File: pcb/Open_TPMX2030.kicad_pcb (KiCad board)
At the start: 0 parts

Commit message: feat: Adjusting the project for a successful start
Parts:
- added D1: 1N4148W, Diode_SMD:D_SOD-123, F.Cu at (146.2, 81.0)
- added G***: LOGO, Open_TPMX2030:Artilect-Logo_12x19mm, F.Cu at (160.0, 82.5)
- added SW1: SW_Push, PCM_Switch_Keyboard_Hotswap_Kailh:SW_Hotswap_Kailh_Choc_V1V2_1.00u, F.Cu at (146.0, 65.0)
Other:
- board outline added: 250 x 102 mm
- copper layers 0 -> 2

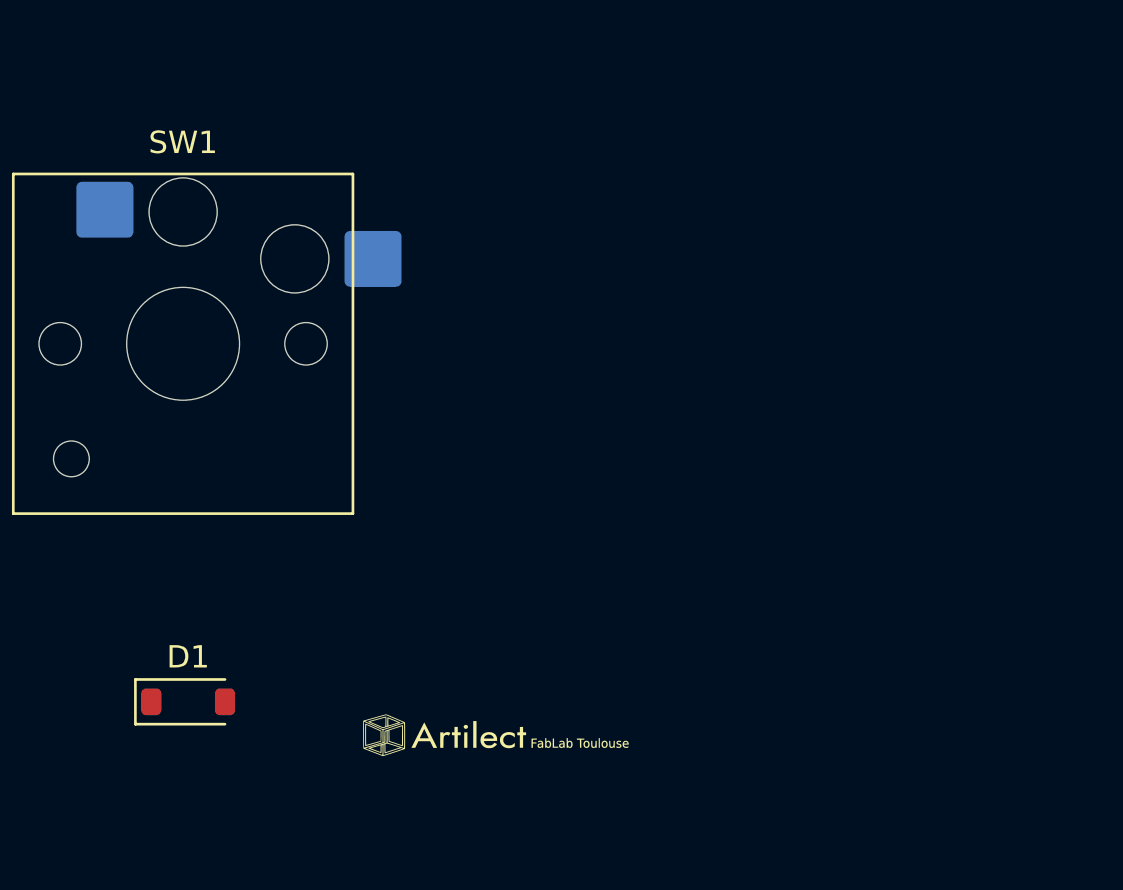
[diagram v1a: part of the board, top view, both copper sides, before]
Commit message: feat: place two switch version for testing
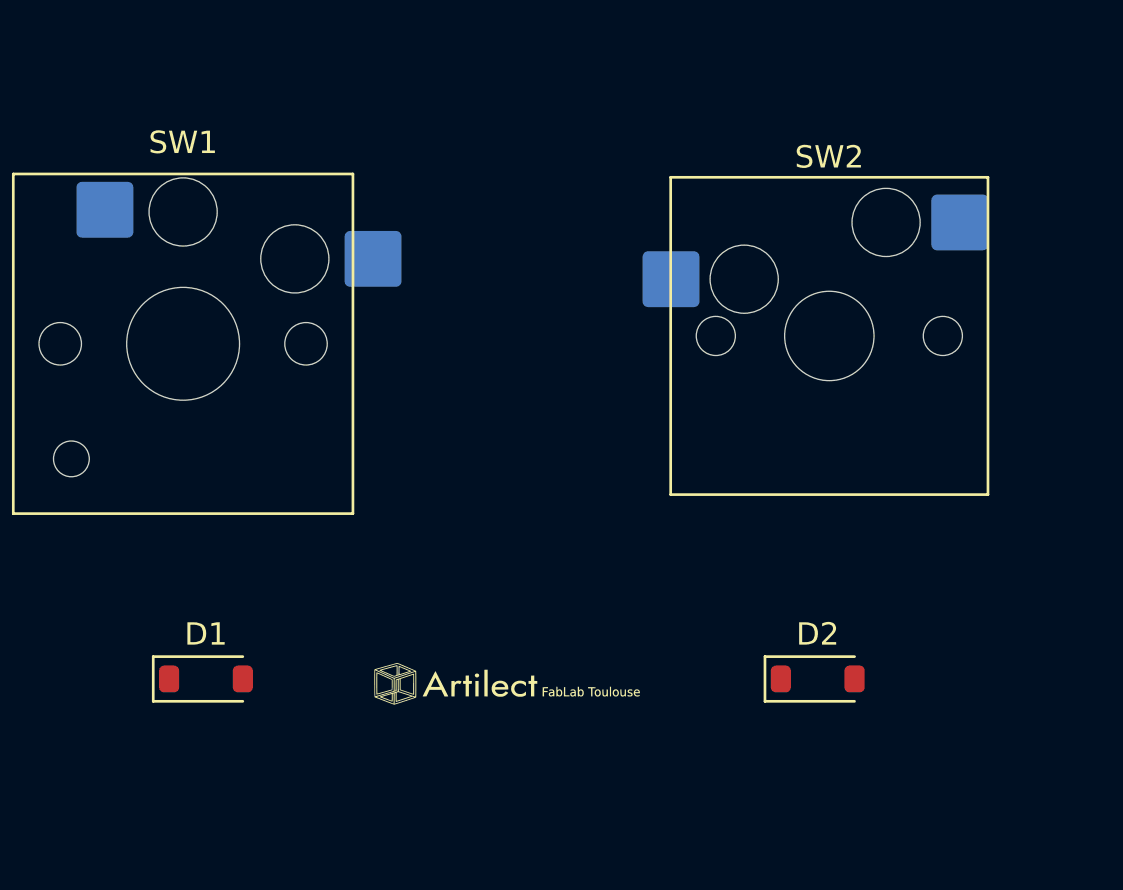
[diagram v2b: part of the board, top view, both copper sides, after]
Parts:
- added D2: 1N4148W, Diode_SMD:D_SOD-123, F.Cu at (174.4, 80.0)
- added SW2: SW_Push, PCM_Switch_Keyboard_Hotswap_Kailh:SW_Hotswap_Kailh_MX_1.00u, F.Cu at (174.9, 64.6)
- moved G*** 2.35 mm to (160.5, 80.2)
- moved D1 1.30 mm to (147.0, 80.0)
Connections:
- D1 pad 1: unconnected-(D1-K-Pad1) -> Net-(D1-K)
- D1 pad 2: unconnected-(D1-A-Pad2) -> Net-(D1-A)
- SW1 pad 1: unconnected-(SW1-Pad1) -> Net-(D1-A)
